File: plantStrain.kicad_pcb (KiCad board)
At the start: 2 copper layers, 76.2 x 19 mm, 20 parts, among them U1 ATtiny85-20MU

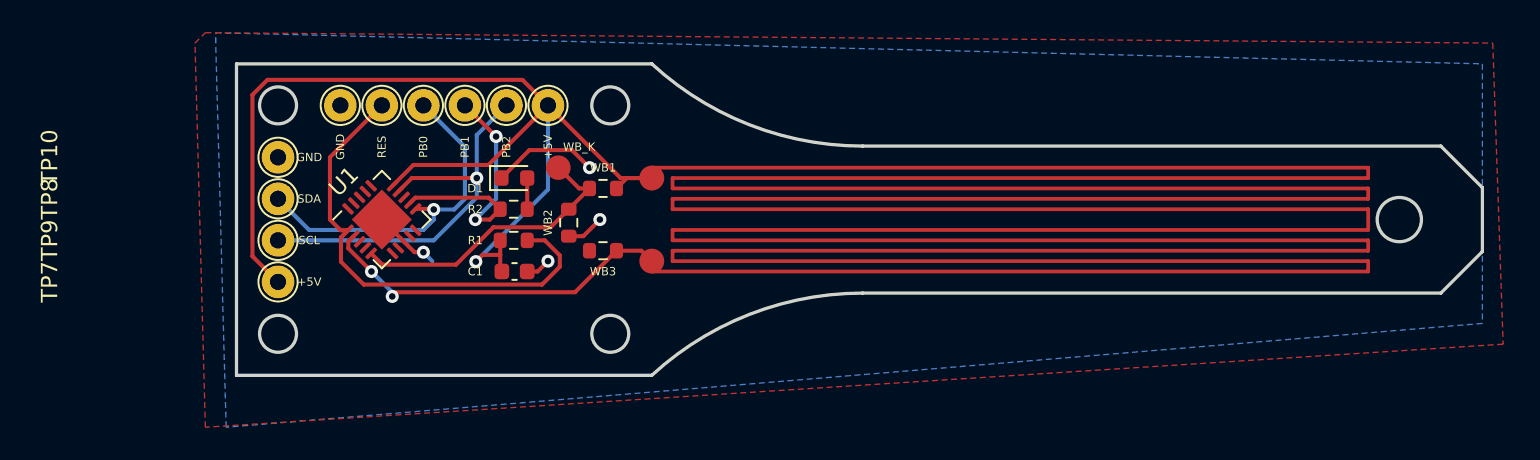
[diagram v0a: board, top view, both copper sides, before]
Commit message: Started updating the board for the strain gauge. Removed unused components and started placing the new ones. Next step is routing.
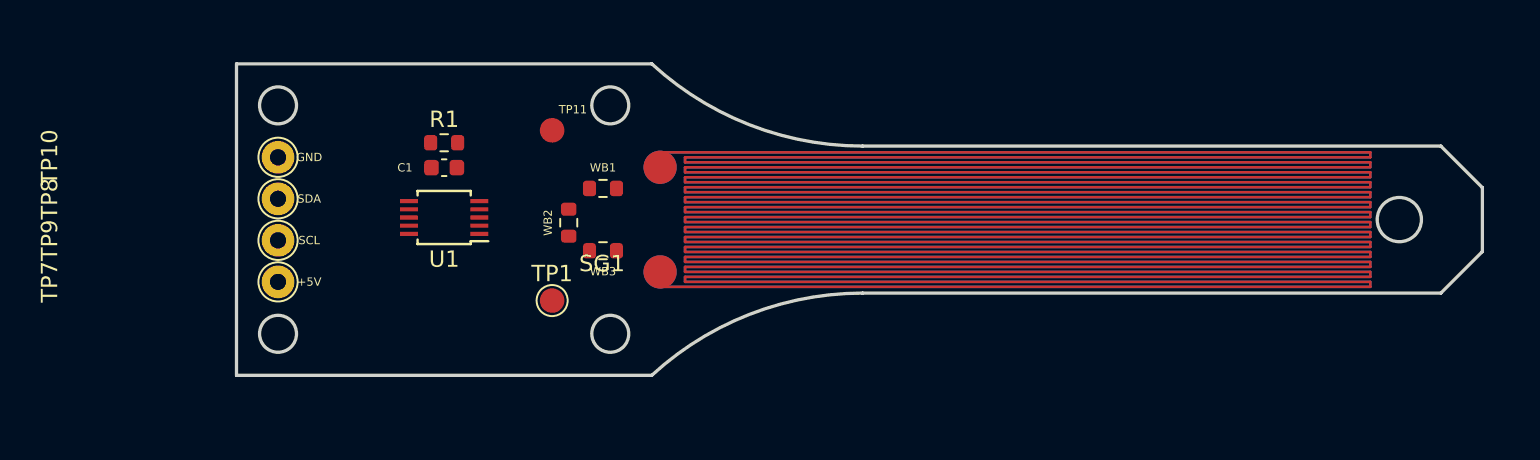
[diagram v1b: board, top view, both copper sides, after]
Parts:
- removed D1: LED, LED_SMD:LED_0603_1608Metric
- removed R2: 220, Resistor_SMD:R_0603_1608Metric
- removed TP2: RES_PROG, TestPoint:TestPoint_THTPad_D2.0mm_Drill1.0mm
- removed TP3: PB0_PROG, TestPoint:TestPoint_THTPad_D2.0mm_Drill1.0mm
- removed TP4: PB1_PROG, TestPoint:TestPoint_THTPad_D2.0mm_Drill1.0mm
- removed TP5: PB2_PROG, TestPoint:TestPoint_THTPad_D2.0mm_Drill1.0mm
- removed TP6: GND_PROG, TestPoint:TestPoint_THTPad_D2.0mm_Drill1.0mm
- added SG2: Strain_Gauge, Arne_Strain:strainLonger, B.Cu at (134.1, 36.2)
- R1: value 10k -> 50
- SG1: footprint Arne_Strain:Strain_Gauge -> Arne_Strain:strainLonger
- TP1: value 5V_PROG -> SG_WB; footprint TestPoint:TestPoint_THTPad_D2.0mm_Drill1.0mm -> TestPoint:TestPoint_Pad_D1.5mm
- U1: value ATtiny85-20MU -> ADS1015IDGS; footprint Package_DFN_QFN:QFN-20-1EP_4x4mm_P0.5mm_EP2.6x2.6mm -> Package_SO:TSSOP-10_3x3mm_P0.5mm
- moved SG1 19.6 mm to (134.1, 36.2)
- moved TP1 11.9 mm to (126.0, 41.1)
- moved C1 7.67 mm to (119.4, 33.0)
- moved R1 7.33 mm to (119.4, 31.5), turned to 0 degrees
- moved U1 3.81 mm to (119.4, 36.1), turned to 180 degrees
- moved TP11 2.32 mm to (126.0, 30.7)
- renumbered WB_K to TP11
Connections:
- R1 pad 1: RES -> +5V
- R1 pad 2: +5V -> Net-(R1-Pad2)
- SG1 pad 1: +5V -> Net-(R1-Pad2)
- SG1 pad 2: Net-(SG1-Pad2) -> SG
- TP1 pad 1: +5V -> SG
- TP11 pad 1: Net-(TP11-Pad1) -> WB_REF
- U1 pad 1: RES -> Net-(U1-Pad1)
- U1 pad 10: Net-(U1-Pad10) -> SCL
- U1 pad 2: Net-(SG1-Pad2) -> Net-(U1-Pad2)
- U1 pad 3: Net-(U1-Pad3) -> GND
- U1 pad 4: Net-(U1-Pad4) -> WB_REF
- U1 pad 5: Net-(TP11-Pad1) -> SG
- U1 pad 8: GND -> +5V
- U1 pad 9: Net-(U1-Pad9) -> SDA
- WB1 pad 1: +5V -> Net-(R1-Pad2)
- WB1 pad 2: Net-(TP11-Pad1) -> WB_REF
- WB2 pad 1: Net-(TP11-Pad1) -> WB_REF
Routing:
- net +5V: track 68.3 -> 0.00 mm, vias 1 -> 0
- net RES: track 29.6 -> 0.00 mm
- net SCL: track 25.3 -> 0.00 mm, vias 1 -> 0
- net Net-(SG1-Pad2): track 22.4 -> 0.00 mm, vias 2 -> 0
- net SDA: track 21.3 -> 0.00 mm, vias 1 -> 0
- net Net-(TP11-Pad1): track 18.0 -> 0.00 mm
- net PB1: track 16.0 -> 0.00 mm, vias 2 -> 0
- net GND: track 15.3 -> 0.00 mm, vias 4 -> 0
- net Net-(D1-Pad2): track 1.91 -> 0.00 mm
- removed copper zone on B.Cu, net GND
- removed copper zone on F.Cu, net GND
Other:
- board text removed: "PB0"
- board text removed: "PB1"
- board text removed: "PB2"
- board text removed: "RES"

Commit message: Routed new board. Needs some more attention to the silkscreen layers to make it easy to use.
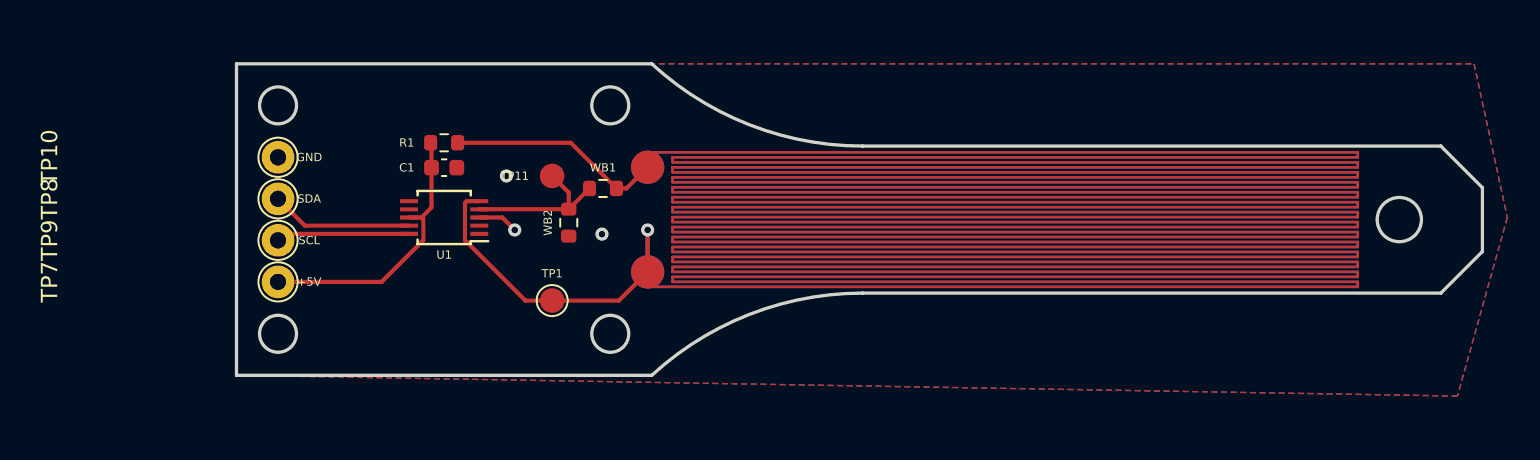
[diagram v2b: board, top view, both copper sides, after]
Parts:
- removed WB3: R_US, Resistor_SMD:R_0603_1608Metric
- moved TP11 2.79 mm to (126.0, 33.5)
- moved SG1 0.76 mm to (133.3, 36.2)
- moved SG2 0.76 mm to (133.3, 36.2)
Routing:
- net SG: track 0.00 -> 21.8 mm, vias 0 -> 1
- net +5V: track 0.00 -> 17.0 mm
- net Net-(R1-Pad2): track 0.00 -> 13.3 mm
- net WB_REF: track 0.00 -> 9.72 mm
- net SDA: track 0.00 -> 8.69 mm
- net SCL: track 0.00 -> 8.17 mm
- net GND: track 0.00 -> 2.48 mm, vias 0 -> 3
- added copper zone on B.Cu, net GND
- added copper zone on F.Cu, net GND
